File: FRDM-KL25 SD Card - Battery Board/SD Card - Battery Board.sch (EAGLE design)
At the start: 77 parts, among them J10 SSW-103-02-S-S, J11 SSW-102-02-S-S, J12 SSW-103-02-S-S, J13 SSW-103-02-S-S, J14 SSW-103-02-S-S, J15 SSW-103-02-S-S, J16 SSW-103-02-S-S, J17 SSW-103-02-S-S, J18 SSW-103-02-S-S, J19 501568-0207-V2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

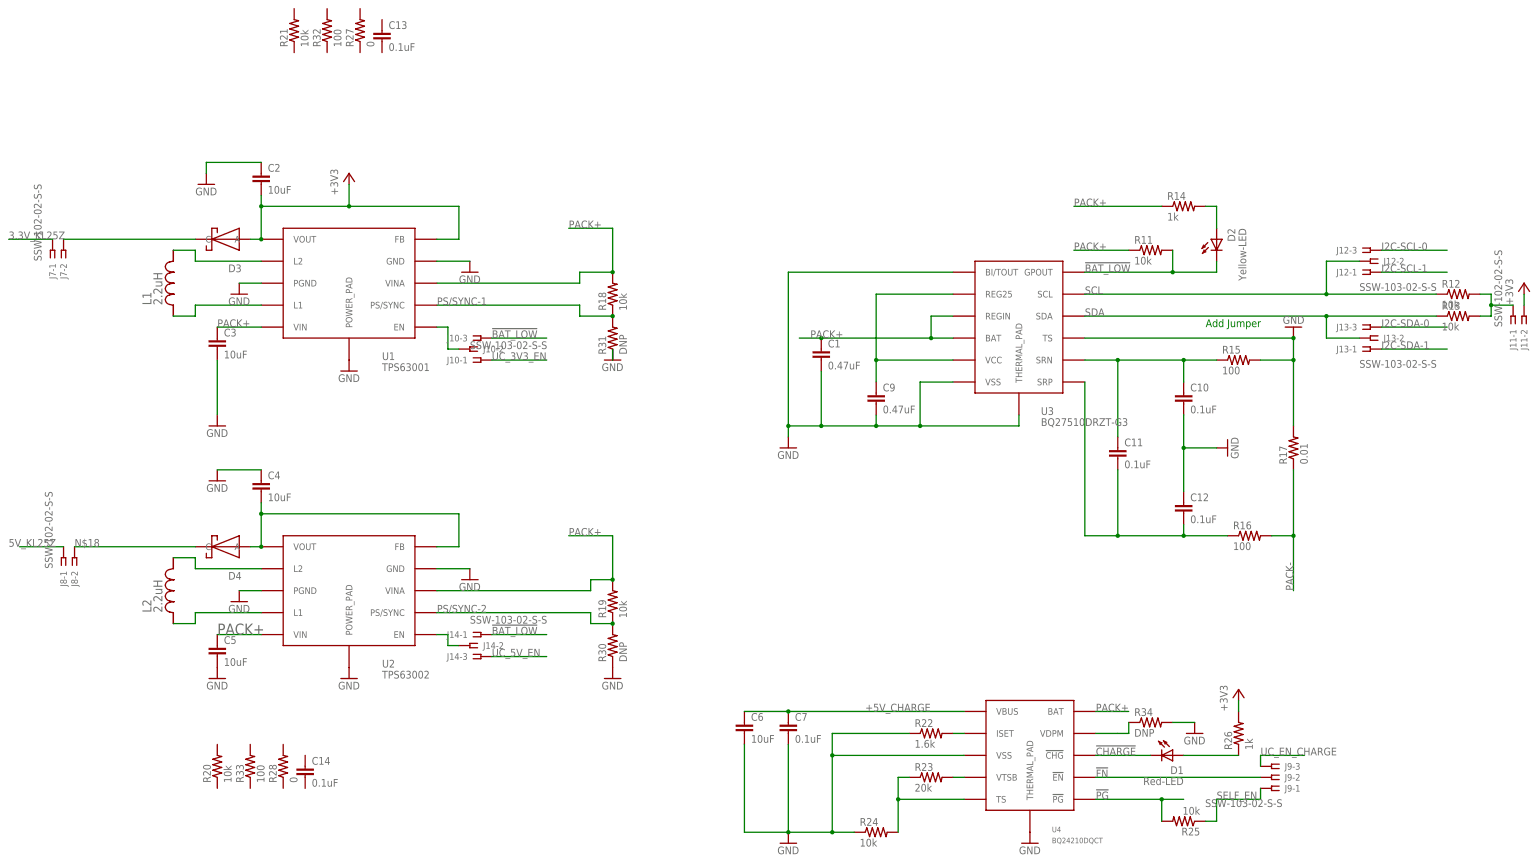
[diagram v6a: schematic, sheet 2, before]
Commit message: FRDM-KL25z-I: Moved power for SD card from +3V3 (before schottky diode) to +3V3-SD (after schottky). Moved 3 pin header a few mil down from USB connector to prevent component interferance
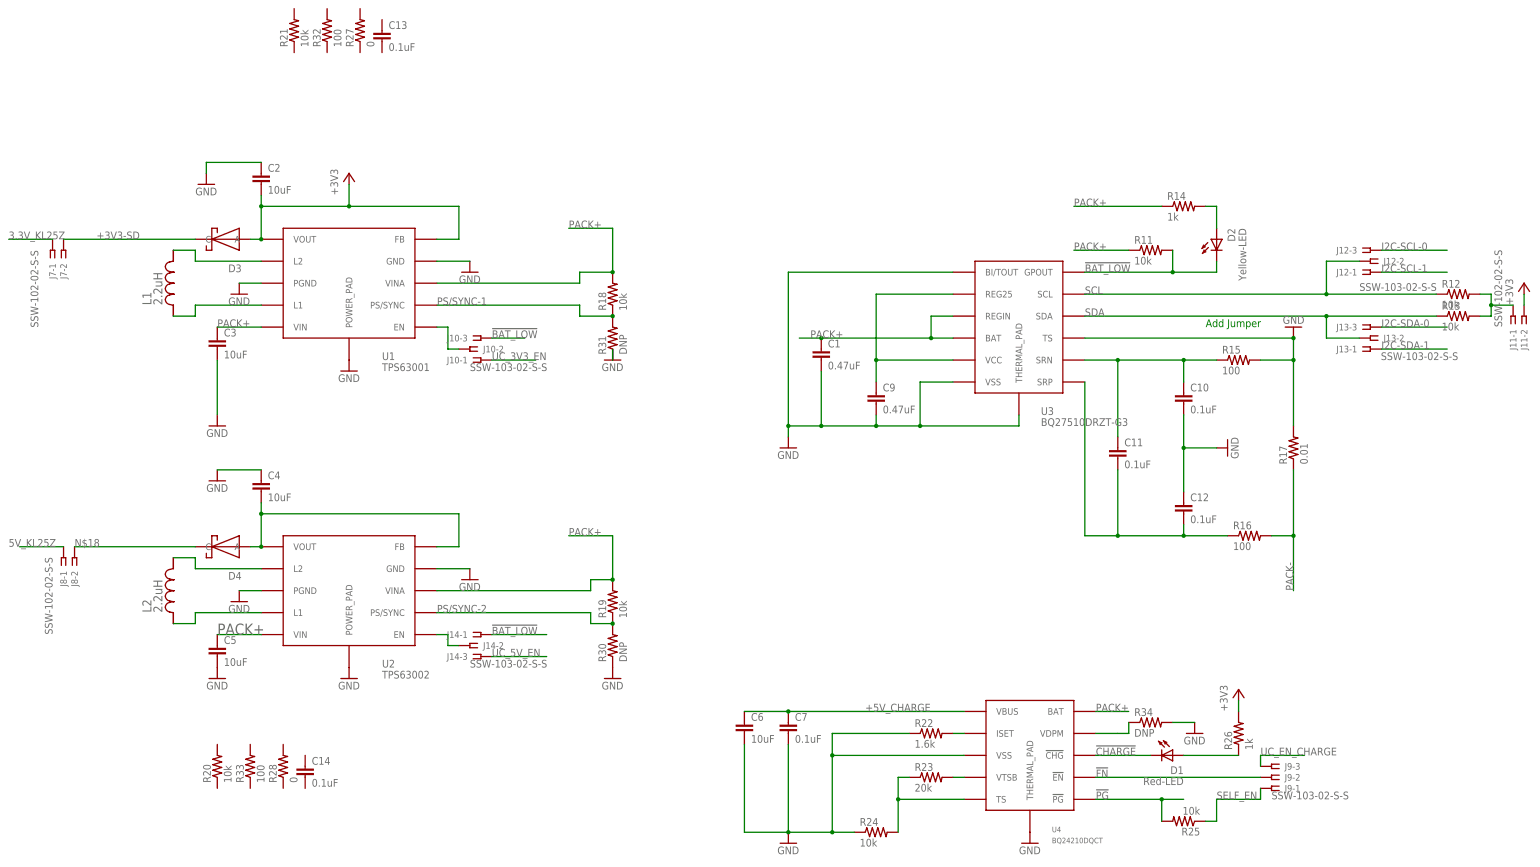
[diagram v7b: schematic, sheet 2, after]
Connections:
- removed net N$17: D3.C, J7-2.1
- new net +3V3-SD: C8.1, D3.C, J1.VDD, J7-2.1, R1.2, R2.2, R3.2, R4.2, R5.2, R6.2, R7.2, R8.2
- net +3V3: no longer C8.1, J1.VDD, R1.2, R2.2, R3.2, R4.2, R5.2, R6.2, R7.2, R8.2

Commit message: FRDM-KL25Z-I: All connections have been completed besides ground. Issue #50 is resolved with SD-CS-A/B implemented, Issue #51 is resolved with UC_3V3_EN being connected to pin J5-3, Issue #52 is resolved with UC_5V_EN connected to pin J5-5, Issue #53 is resolved with UC_EN_CHARGE being connected to pin J5-1. The Card detect as well as write protect lines from the SD card have also been broken out and connected.
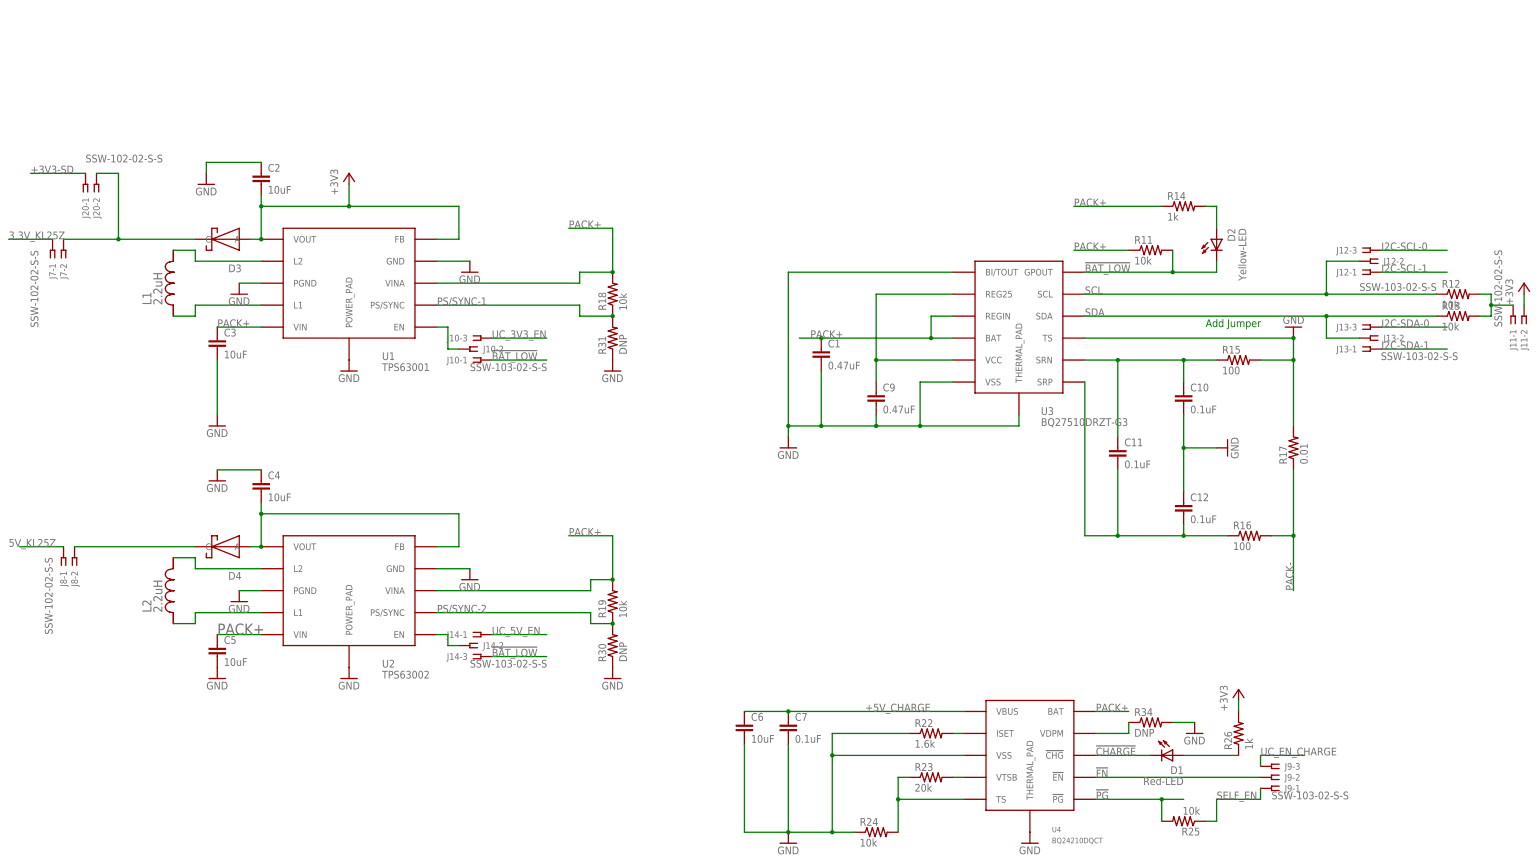
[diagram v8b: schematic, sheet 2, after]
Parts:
- removed C13, C14: 0.1uF, Kas-Capacitors:CAPACITOR0.1U-X7R-10%-25V
- removed R20, R21: 10k, Kas-Resistors:RESISTOR10K-62.5M-1%-50V
- removed R27, R28: 0, Kas-Resistors:RESISTOR0-100M-X%-50V
- removed R32, R33: 100, Kas-Resistors:RESISTOR1K-63M-1%-50V-0402
- added J20: SSW-102-02-S-S, Kas-Connectors:SSW-102-02-S-S
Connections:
- new net N$17: D3.C, J20-2.1, J7-2.1
- net !BAT_LOW: now also J10-1.1, J14-3.1; no longer J10-3.1, J14-1.1
- net +3V3-SD: now also J20-1.1; no longer D3.C, J7-2.1
- net SD-CARD-DETECT: now also J6-1.1
- net SD-WRITE-PROTECT: now also J6-3.1
- net SPI-CSB-SD-A: now also J5-11.1
- net SPI-CSB-SD-B: now also J5-15.1
- net UC_3V3_EN: now also J10-3.1, J5-3.1; no longer J10-1.1
- net UC_5V_EN: now also J14-1.1, J5-5.1; no longer J14-3.1
- net UC_EN_CHARGE: now also J5-1.1
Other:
- note removed: "TPS6300x Data Sheet"
- moved on the sheet: C8, J18-1, J18-2, J18-3
